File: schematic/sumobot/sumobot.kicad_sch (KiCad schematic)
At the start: 6 parts, among them J1 Screw_Terminal_01x02, J2 Screw_Terminal_01x02, J3 Screw_Terminal_01x02, J4 Conn_01x05, U1 ROB-14450

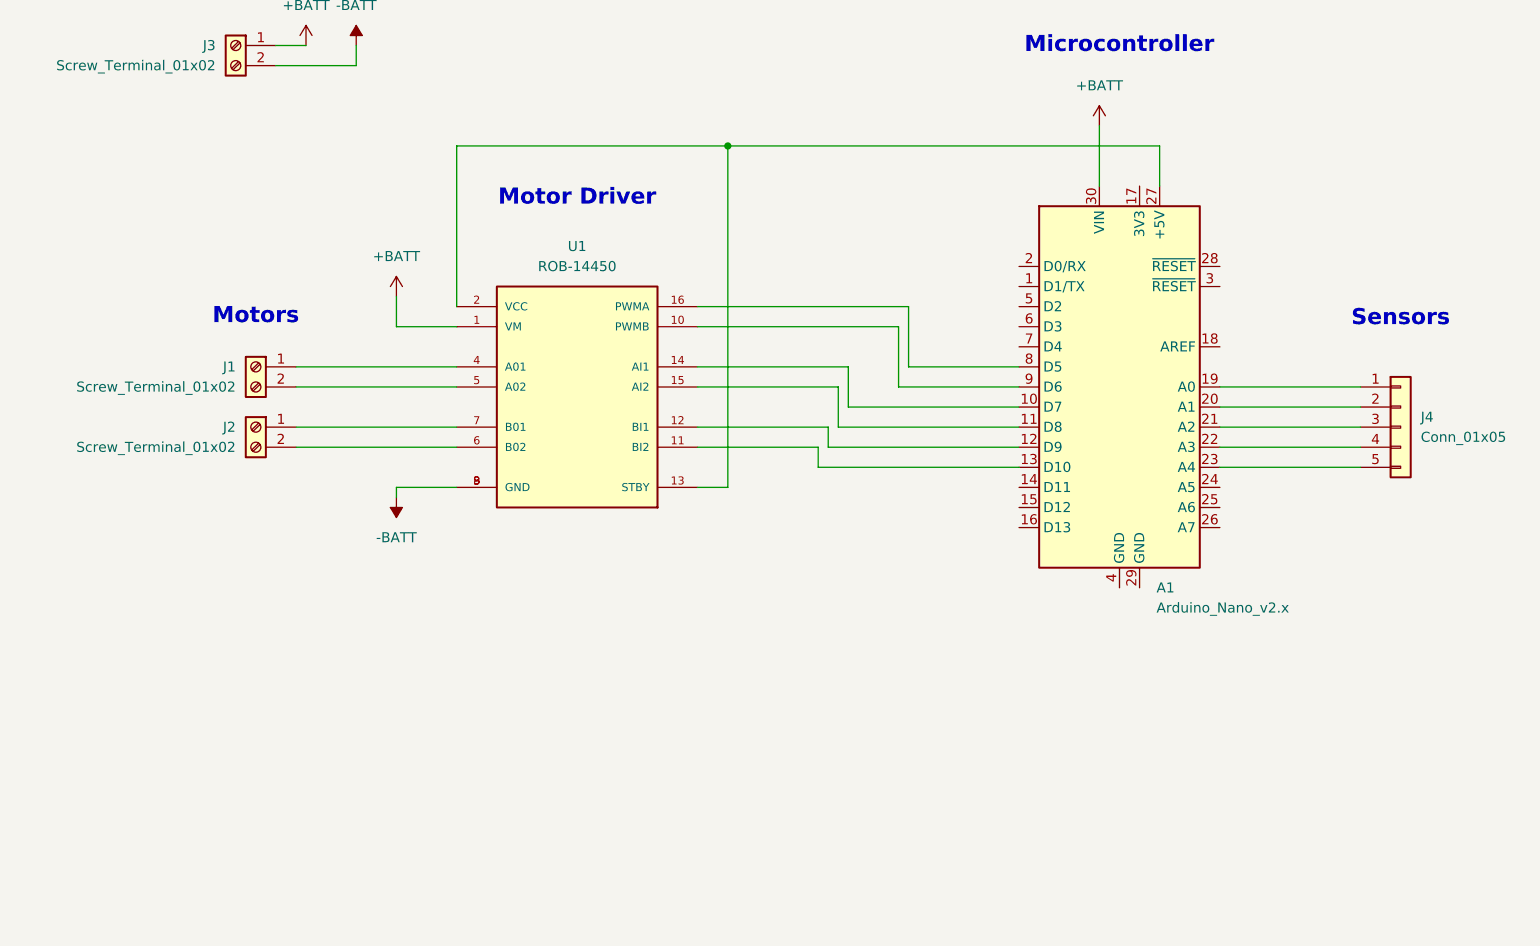
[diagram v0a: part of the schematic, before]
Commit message: fix: update net names and add junctions in schematic and PCB for improved connectivity
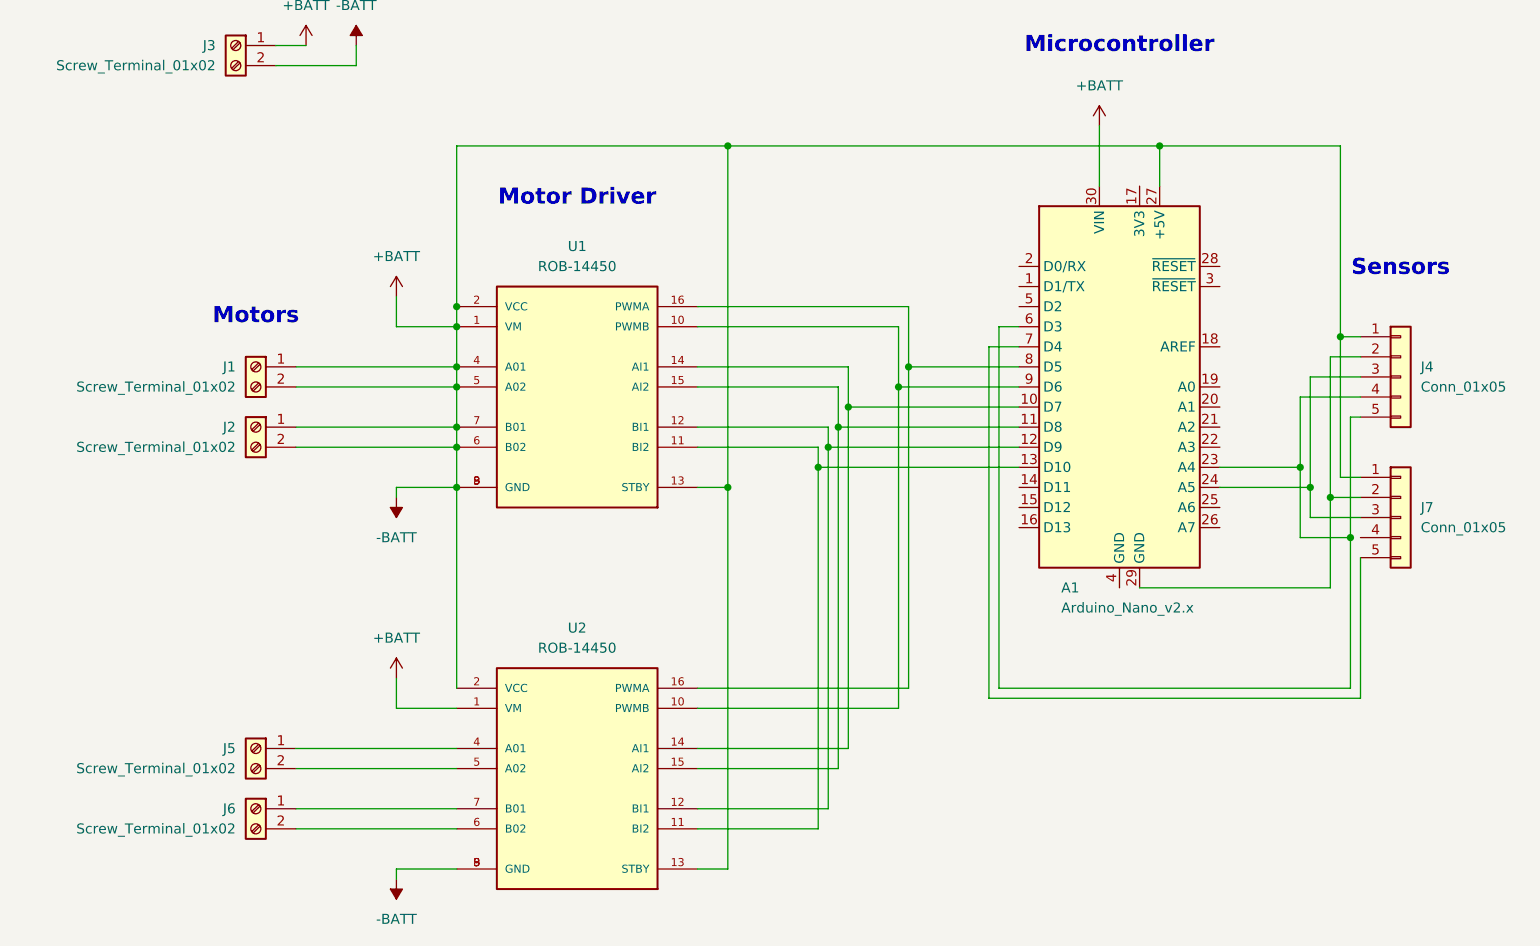
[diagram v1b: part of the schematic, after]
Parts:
- added J5, J6: Screw_Terminal_01x02, TerminalBlock:TerminalBlock_MaiXu_MX126-5.0-02P_1x02_P5.00mm, symbol Connector:Screw_Terminal_01x02
- added J7: Conn_01x05, Connector_PinHeader_1.00mm:PinHeader_1x05_P1.00mm_Vertical, symbol Connector_Generic:Conn_01x05
- added U2: ROB-14450, TB6612FNG:MODULE_ROB-14450, symbol ROB-14450:ROB-14450
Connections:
- net -BATT is gone; now on net +BATT: J3.2 (Pin_2), U1.3 (GND), U1.8 (GND), U1.9 (GND)
- net +BATT: now also A1.27 (+5V), J1.1 (Pin_1), J1.2 (Pin_2), J2.1 (Pin_1), J2.2 (Pin_2), J4.1 (Pin_1), U1.13 (STBY), U1.2 (VCC), U1.4 (A01), U1.5 (A02), U1.6 (B02), U1.7 (B01), J7.1 (Pin_1), U2.1 (VM), U2.13 (STBY), U2.2 (VCC), U2.3 (GND), U2.8 (GND), U2.9 (GND)
- net at A1.9 (D6), U1.10 (PWMB): now also U2.10 (PWMB)
- net at A1.13 (D10), U1.11 (BI2): now also U2.11 (BI2)
- net at A1.12 (D9), U1.12 (BI1): now also U2.12 (BI1)
- net at A1.10 (D7), U1.14 (AI1): now also U2.14 (AI1)
- net at A1.11 (D8), U1.15 (AI2): now also U2.15 (AI2)
- net at A1.8 (D5), U1.16 (PWMA): now also U2.16 (PWMA)
- net at A1.19 (A0): no longer J4.1 (Pin_1)
- net at J4.2 (Pin_2): now also A1.29 (GND), J7.2 (Pin_2); no longer A1.20 (A1)
- net at J4.3 (Pin_3): now also A1.24 (A5), J7.3 (Pin_3); no longer A1.21 (A2)
- net at J4.4 (Pin_4): now also A1.23 (A4), A1.6 (D3), J4.5 (Pin_5); no longer A1.22 (A3)
- net at A1.7 (D4): now also J7.5 (Pin_5)
- new net: J6.1 (Pin_1), U2.7 (B01)
- new net: J6.2 (Pin_2), U2.6 (B02)
- new net: J5.1 (Pin_1), U2.4 (A01)
- new net: J5.2 (Pin_2), U2.5 (A02)
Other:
- moved on the sheet: J4

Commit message: haha
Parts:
- removed J1, J2, J5, J6: Screw_Terminal_01x02, TerminalBlock:TerminalBlock_MaiXu_MX126-5.0-02P_1x02_P5.00mm, symbol Connector:Screw_Terminal_01x02
- added SW1: Switch, symbol ScottoKeebs:Placeholder_Switch
- added SW2: SW_DIP_x04, symbol Switch:SW_DIP_x04
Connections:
- net +BATT: now also SW2.1; no longer A1.27 (+5V), A1.30 (VIN), J3.2 (Pin_2), J4.1 (Pin_1), J7.1 (Pin_1), U1.1 (VM), U1.13 (STBY), U1.2 (VCC), U1.3 (GND), U1.4 (A01), U1.5 (A02), U1.6 (B02), U1.7 (B01), U1.8 (GND), U1.9 (GND), U2.1 (VM), U2.13 (STBY), U2.2 (VCC), U2.3 (GND), U2.8 (GND), U2.9 (GND)
- net at U1.11 (BI2), U2.11 (BI2): now also A1.11 (D8); no longer A1.13 (D10)
- net at U1.12 (BI1), U2.12 (BI1): now also A1.10 (D7); no longer A1.12 (D9)
- net at U1.14 (AI1), U2.14 (AI1): now also A1.6 (D3); no longer A1.10 (D7)
- net at U1.15 (AI2), U2.15 (AI2): now also A1.7 (D4); no longer A1.11 (D8)
- net at A1.23 (A4), J4.4 (Pin_4), J4.5 (Pin_5): now also A1.1 (D1/TX); no longer A1.6 (D3)
- net at A1.14 (D11): now also SW2.7
- net at A1.15 (D12): now also SW1.2
- net at A1.2 (D0/RX): now also J7.5 (Pin_5)
- new net: A1.30 (VIN), SW2.8, U1.1 (VM), U2.1 (VM)
- new net: A1.27 (+5V), J4.1 (Pin_1), J7.1 (Pin_1), U1.13 (STBY), U1.2 (VCC), U2.13 (STBY), U2.2 (VCC)
- new net: A1.12 (D9), SW2.5
- new net: A1.13 (D10), SW2.6
- new net -BATT: J3.2 (Pin_2), SW1.1, SW2.2, SW2.3, SW2.4, U1.3 (GND), U1.8 (GND), U1.9 (GND), U2.3 (GND), U2.8 (GND), U2.9 (GND)
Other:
- note added: "Controls"

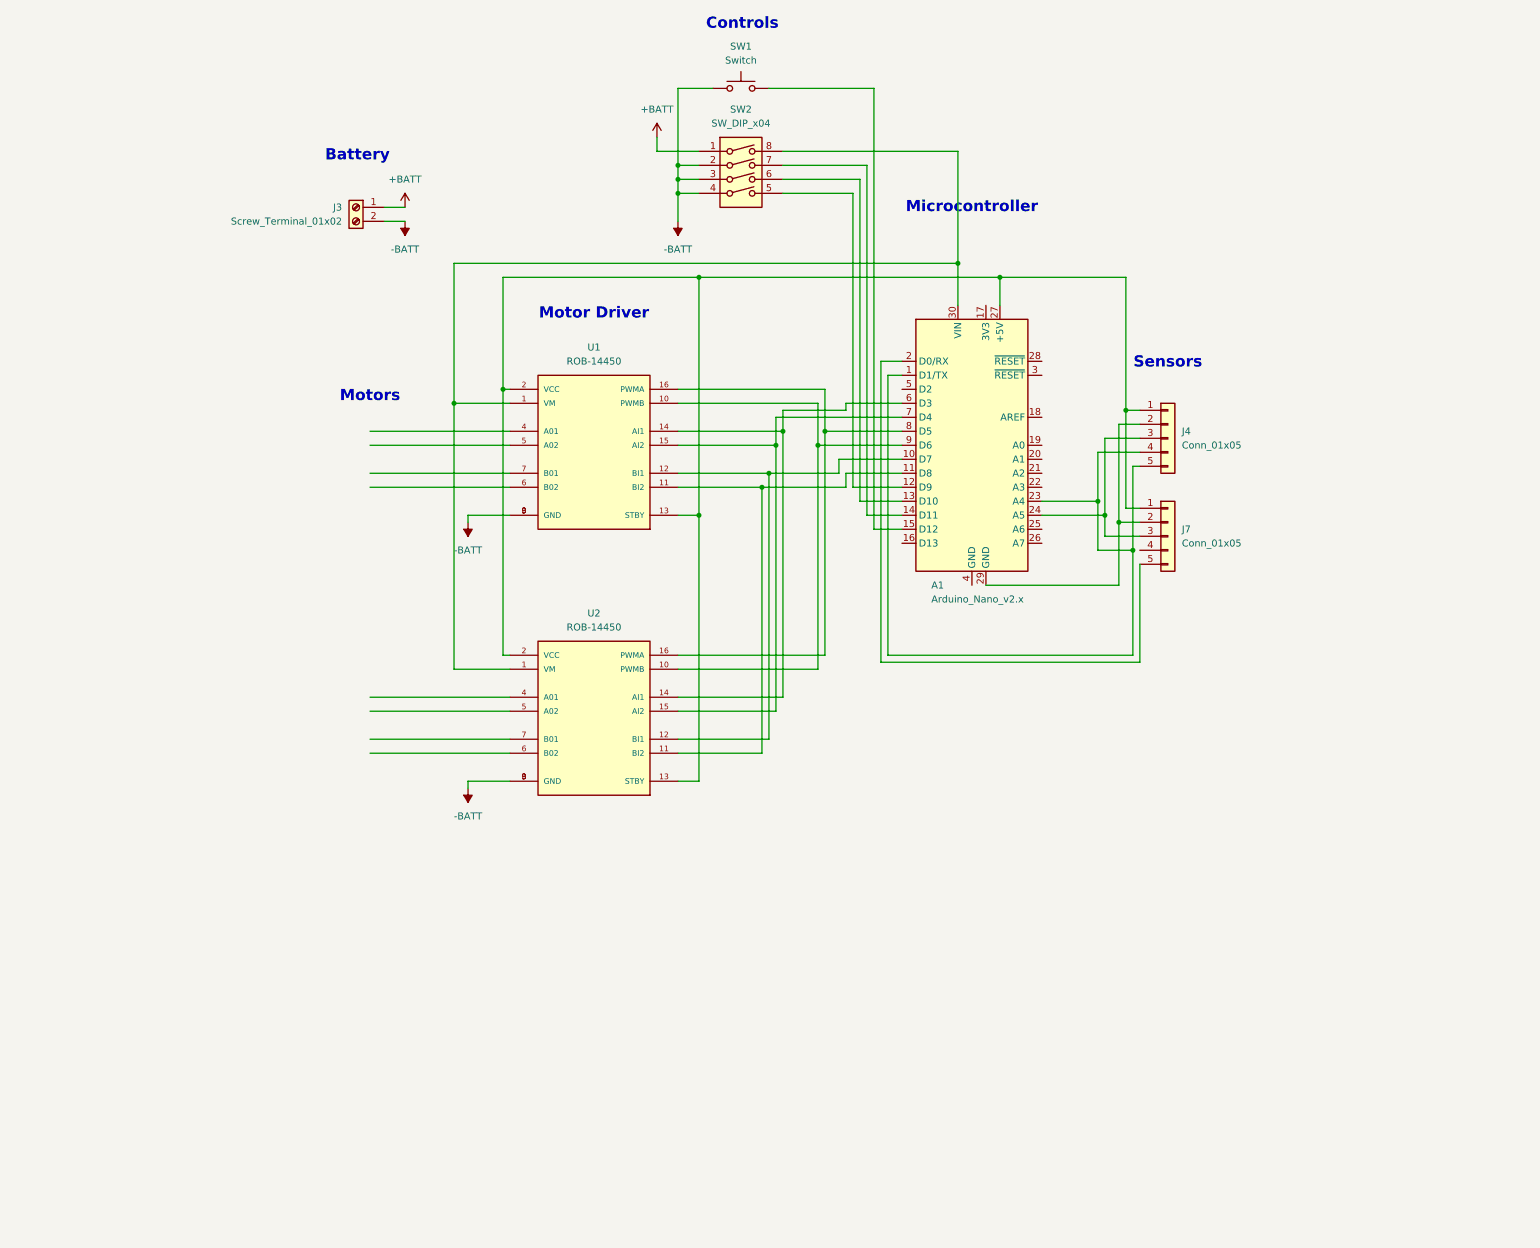
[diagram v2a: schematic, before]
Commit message: feat: add new 3D models and schematic
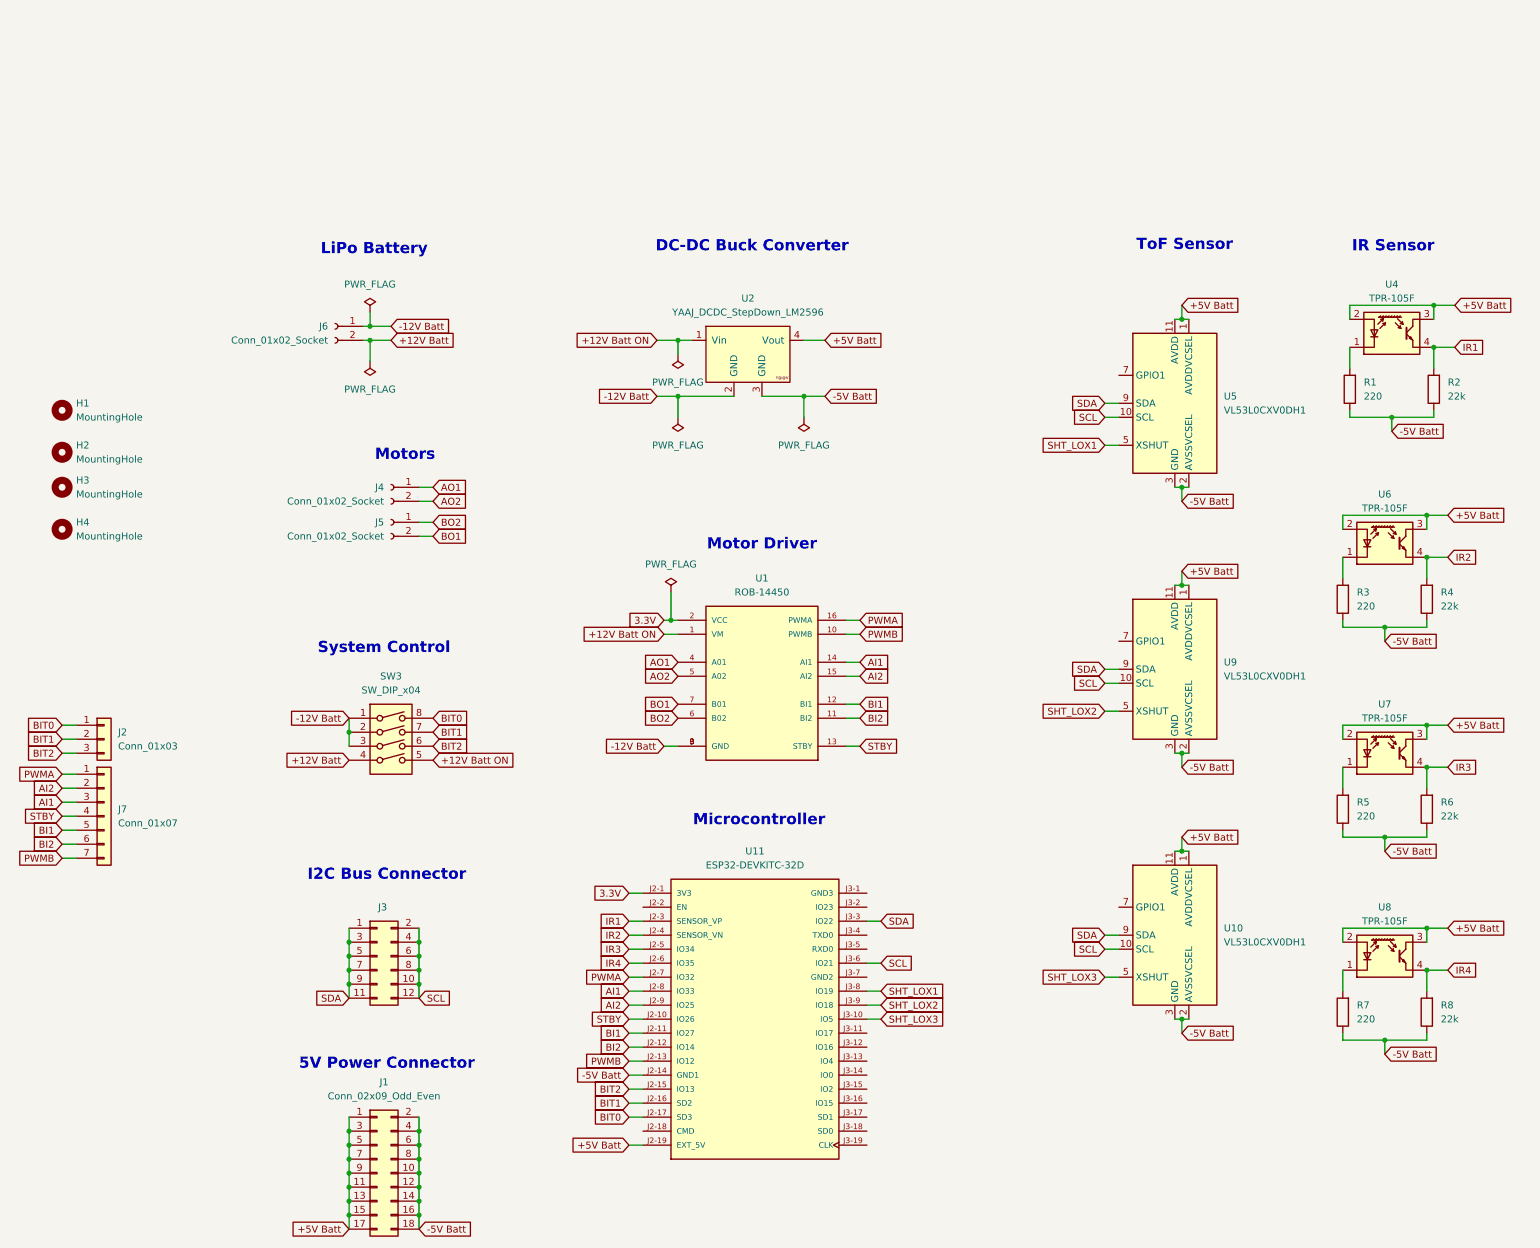
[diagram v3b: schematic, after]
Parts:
- removed A1: Arduino_Nano_v2.x, Module:Arduino_Nano, symbol MCU_Module:Arduino_Nano_v2.x
- removed J3: Screw_Terminal_01x02, TerminalBlock:TerminalBlock_MaiXu_MX126-5.0-02P_1x02_P5.00mm, symbol Connector:Screw_Terminal_01x02
- removed J4, J7: Conn_01x05, Connector_PinHeader_1.00mm:PinHeader_1x05_P1.00mm_Vertical, symbol Connector_Generic:Conn_01x05
- removed SW1: Switch, symbol ScottoKeebs:Placeholder_Switch
- removed SW2: SW_DIP_x04, symbol Switch:SW_DIP_x04
- removed U2: ROB-14450, TB6612FNG:MODULE_ROB-14450, symbol ROB-14450:ROB-14450
- added H1, H2, H3, H4: MountingHole, MountingHole:MountingHole_2.5mm, symbol Mechanical:MountingHole
- added J1: Conn_02x09_Odd_Even, Connector_PinHeader_2.54mm:PinHeader_2x09_P2.54mm_Vertical, symbol Connector_Generic:Conn_02x09_Odd_Even
- added J2: Conn_01x03, Connector_PinHeader_2.54mm:PinHeader_1x03_P2.54mm_Vertical, symbol Connector_Generic:Conn_01x03
- added J3: Conn_02x06_Counter_Clockwise, Connector_PinHeader_2.54mm:PinHeader_2x06_P2.54mm_Vertical, symbol Connector_Generic:Conn_02x06_Odd_Even
- added J4, J5, J6: Conn_01x02_Socket, Connector_JST:JST_XH_B2B-XH-A_1x02_P2.50mm_Vertical, symbol Connector:Conn_01x02_Socket
- added J7: Conn_01x07, Connector_PinHeader_2.54mm:PinHeader_1x07_P2.54mm_Vertical, symbol Connector_Generic:Conn_01x07
- added R1, R3, R5, R7: 220, symbol ScottoKeebs:Placeholder_Resistor
- added R2, R4, R6, R8: 22k, symbol ScottoKeebs:Placeholder_Resistor
- added SW3: SW_DIP_x04, Button_Switch_THT:SW_DIP_SPSTx04_Slide_9.78x12.34mm_W7.62mm_P2.54mm, symbol Switch:SW_DIP_x04
- added U10, U5, U9: VL53L0CXV0DH1, Sensor_Distance:ST_VL53L1x, symbol Sensor_Distance:VL53L0CXV0DH1
- added U11: ESP32-DEVKITC-32D, ESP32-DEVKITC-32D:MODULE_ESP32-DEVKITC-32D, symbol ESP32-DEVKITC-32D:ESP32-DEVKITC-32D
- added U2: YAAJ_DCDC_StepDown_LM2596, LM2596-Buck-Converter:YAAJ_DCDC_StepDown_LM2596, symbol yaaj_dcdc_stepdown_lm2596:YAAJ_DCDC_StepDown_LM2596
- added U4, U6, U7, U8: TPR-105F, Package_TO_SOT_THT:TO-18-3_Lens, symbol Sensor_Proximity:BPR-205
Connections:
- net +12V Batt ON: now reaches U1.1 (VM)
- net +12V Batt ON: now also SW3.5, U2.1 (Vin)
- net PWMB: now reaches U1.10 (PWMB)
- net PWMB: now also J7.7 (Pin_7), U11.J2-13 (IO12)
- net BI2: now reaches U1.11 (BI2)
- net BI2: now also J7.6 (Pin_6), U11.J2-12 (IO14)
- net BI1: now reaches U1.12 (BI1)
- net BI1: now also J7.5 (Pin_5), U11.J2-11 (IO27)
- net 3.3V: now reaches U1.2 (VCC)
- net 3.3V: now also U11.J2-1 (3V3); no longer U1.13 (STBY)
- net AI1: now reaches U1.14 (AI1)
- net AI1: now also J7.3 (Pin_3), U11.J2-8 (IO33)
- net AI2: now reaches U1.15 (AI2)
- net AI2: now also J7.2 (Pin_2), U11.J2-9 (IO25)
- net PWMA: now reaches U1.16 (PWMA)
- net PWMA: now also J7.1 (Pin_1), U11.J2-7 (IO32)
- net AO1: now reaches U1.4 (A01)
- net AO1: now also J4.1 (Pin_1)
- net AO2: now reaches U1.5 (A02)
- net AO2: now also J4.2 (Pin_2)
- net BO2: now reaches U1.6 (B02)
- net BO2: now also J5.1 (Pin_1)
- net BO1: now reaches U1.7 (B01)
- net BO1: now also J5.2 (Pin_2)
- net -BATT renamed -12V Batt
- net -12V Batt: now also J6.1 (Pin_1), SW3.1, SW3.2, SW3.3, U2.2 (GND)
- new net: R7.2, U8.1 (K)
- new net: R1.2, U4.1 (K)
- new net: R5.2, U7.1 (K)
- new net: R3.2, U6.1 (K)
- new net +12V Batt: J6.2 (Pin_2), SW3.4
- new net +5V Batt: J1.1 (Pin_1), J1.11 (Pin_11), J1.13 (Pin_13), J1.15 (Pin_15), J1.17 (Pin_17), J1.3 (Pin_3), J1.5 (Pin_5), J1.7 (Pin_7), J1.9 (Pin_9), U10.1 (AVDDVCSEL), U10.11 (AVDD), U11.J2-19 (EXT_5V), U2.4 (Vout), U4.2 (A), U4.3 (C), U5.1 (AVDDVCSEL), U5.11 (AVDD), U6.2 (A), U6.3 (C), U7.2 (A), U7.3 (C), U8.2 (A), U8.3 (C), U9.1 (AVDDVCSEL), U9.11 (AVDD)
- new net -5V Batt: J1.10 (Pin_10), J1.12 (Pin_12), J1.14 (Pin_14), J1.16 (Pin_16), J1.18 (Pin_18), J1.2 (Pin_2), J1.4 (Pin_4), J1.6 (Pin_6), J1.8 (Pin_8), R1.1, R2.1, R3.1, R4.1, R5.1, R6.1, R7.1, R8.1, U10.12 (GND), U10.2 (AVSSVCSEL), U10.3 (GND), U10.4 (GND), U10.6 (GND), U11.J2-14 (GND1), U2.3 (GND), U5.12 (GND), U5.2 (AVSSVCSEL), U5.3 (GND), U5.4 (GND), U5.6 (GND), U9.12 (GND), U9.2 (AVSSVCSEL), U9.3 (GND), U9.4 (GND), U9.6 (GND)
- new net BIT0: J2.1 (Pin_1), SW3.8, U11.J2-17 (SD3)
- new net BIT1: J2.2 (Pin_2), SW3.7, U11.J2-16 (SD2)
- new net BIT2: J2.3 (Pin_3), SW3.6, U11.J2-15 (IO13)
- new net IR1: R2.2, U11.J2-3 (SENSOR_VP), U4.4 (E)
- new net IR2: R4.2, U11.J2-4 (SENSOR_VN), U6.4 (E)
- new net IR3: R6.2, U11.J2-5 (IO34), U7.4 (E)
- new net IR4: R8.2, U11.J2-6 (IO35), U8.4 (E)
- new net SCL: J3.10 (Pin_10), J3.12 (Pin_12), J3.2 (Pin_2), J3.4 (Pin_4), J3.6 (Pin_6), J3.8 (Pin_8), U10.10 (SCL), U11.J3-6 (IO21), U5.10 (SCL), U9.10 (SCL)
- new net SDA: J3.1 (Pin_1), J3.11 (Pin_11), J3.3 (Pin_3), J3.5 (Pin_5), J3.7 (Pin_7), J3.9 (Pin_9), U10.9 (SDA), U11.J3-3 (IO22), U5.9 (SDA), U9.9 (SDA)
- new net SHT_LOX1: U11.J3-8 (IO19), U5.5 (XSHUT)
- new net SHT_LOX2: U11.J3-9 (IO18), U9.5 (XSHUT)
- new net SHT_LOX3: U10.5 (XSHUT), U11.J3-10 (IO5)
- new net STBY: J7.4 (Pin_4), U1.13 (STBY), U11.J2-10 (IO26)
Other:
- note added: "5V Power Connector"
- note added: "DC-DC Buck Converter"
- note added: "I2C Bus Connector"
- note added: "IR Sensor"
- note added: "LiPo Battery"
- note added: "System Control"
- note added: "ToF Sensor"
- note removed: "Battery"
- note removed: "Controls"
- note removed: "Sensors"
- moved on the sheet: U1
